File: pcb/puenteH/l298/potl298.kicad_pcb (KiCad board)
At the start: 2 copper layers, 51.1 x 86.2 mm, 19 parts, among them K1 CONN_3, K2 CONN_3, P1 CONN_2X2, P2 PWR, P3 CONN_2, P4 CONN_2, U1 L298

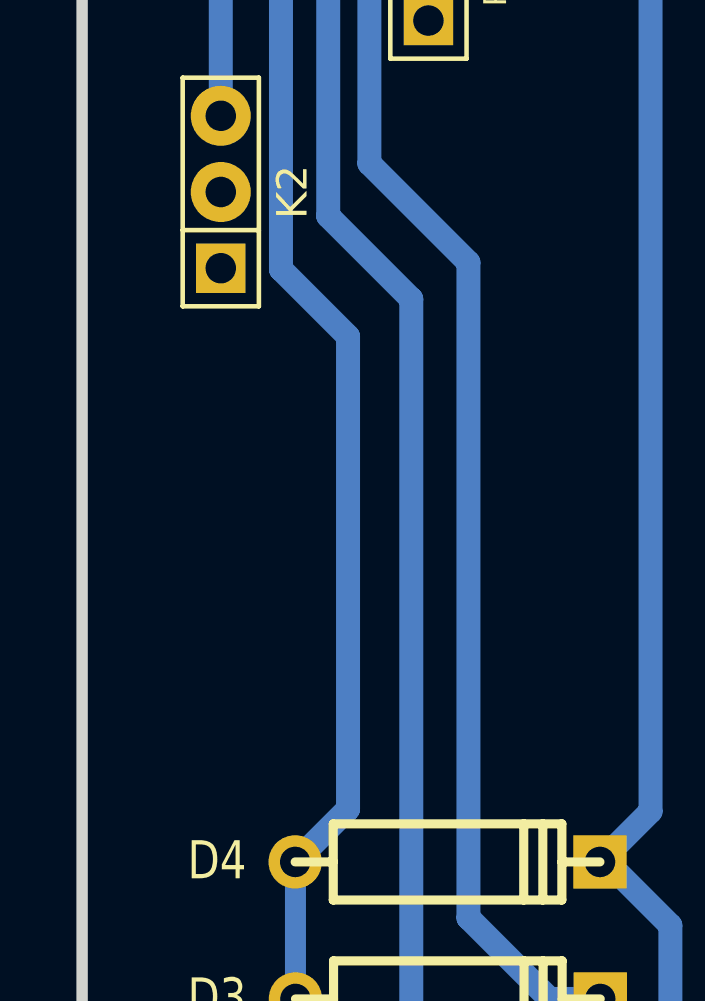
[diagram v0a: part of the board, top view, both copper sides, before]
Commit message: pull down pin Hk 15 and 16 in vertical shield
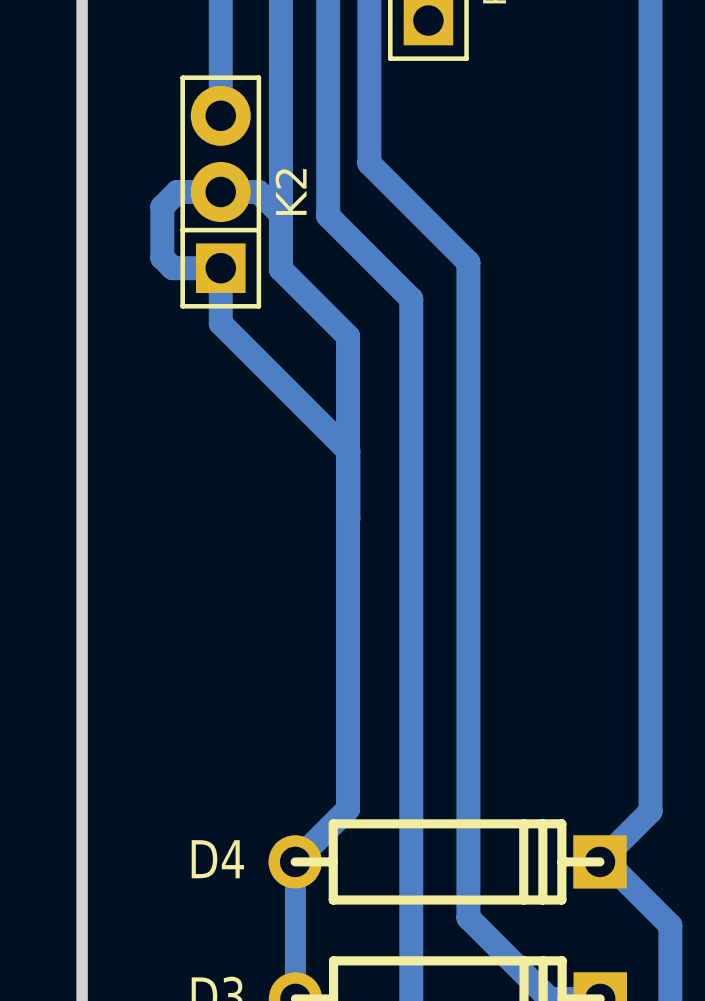
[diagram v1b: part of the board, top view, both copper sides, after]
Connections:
- K1 pad 2: (no net) -> N-0000013
- K2 pad 1: (no net) -> GND
- K2 pad 2: (no net) -> GND
- P3 pad 1: (no net) -> N-000007
- P4 pad 1: (no net) -> N-0000016
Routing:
- net GND: track 200.0 -> 220.2 mm
